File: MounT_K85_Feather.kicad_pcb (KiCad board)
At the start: 2 copper layers, 50.8 x 22.9 mm, 10 parts, among them J1 Adafruit_Feather, J2 DB25_Male, SW1 CUS-12TB, U1 MAX3232

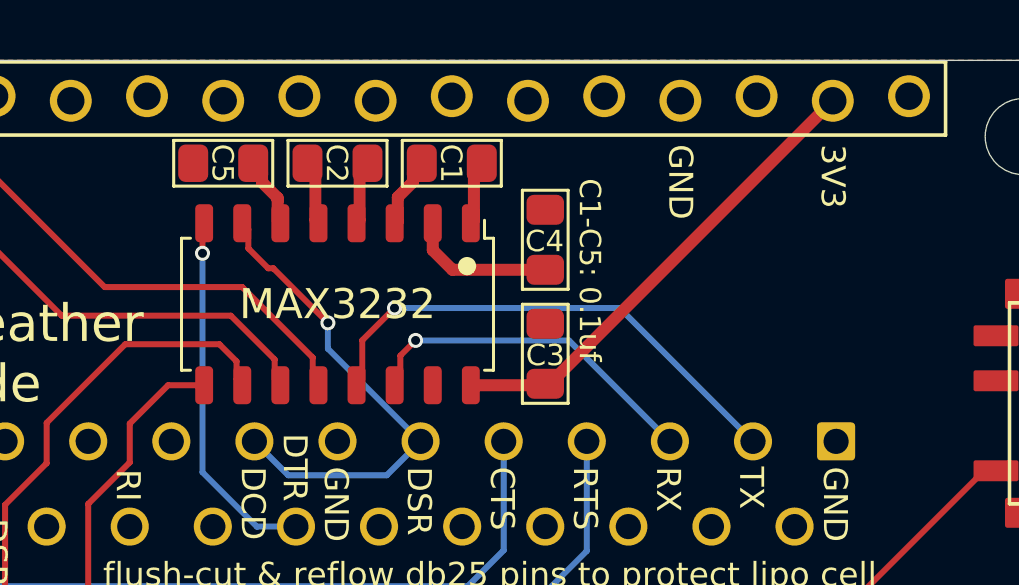
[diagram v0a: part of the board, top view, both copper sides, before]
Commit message: smt power switch on feather, routing 3v3 on teensy, silkscreen all
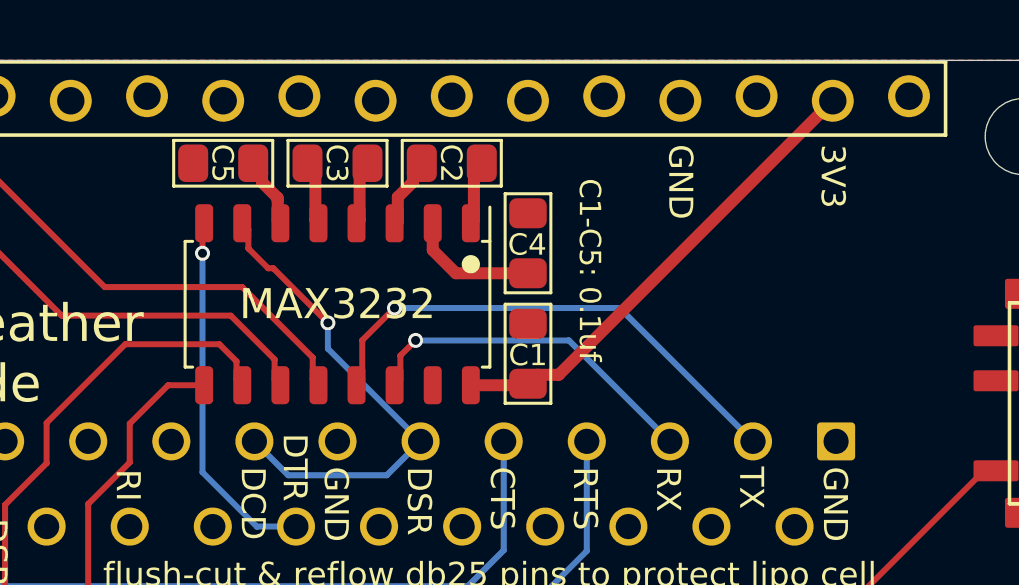
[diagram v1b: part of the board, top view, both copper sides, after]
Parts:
- moved C4 0.59 mm to (153.7, 91.2)
- moved C1 0.58 mm to (153.7, 94.9)
- renumbered C3 to C1, C1 to C2, C2 to C3
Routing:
- net Net-(C4-Pad1): track 4.92 -> 4.39 mm
